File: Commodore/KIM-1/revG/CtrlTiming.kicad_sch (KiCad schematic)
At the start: 22 parts

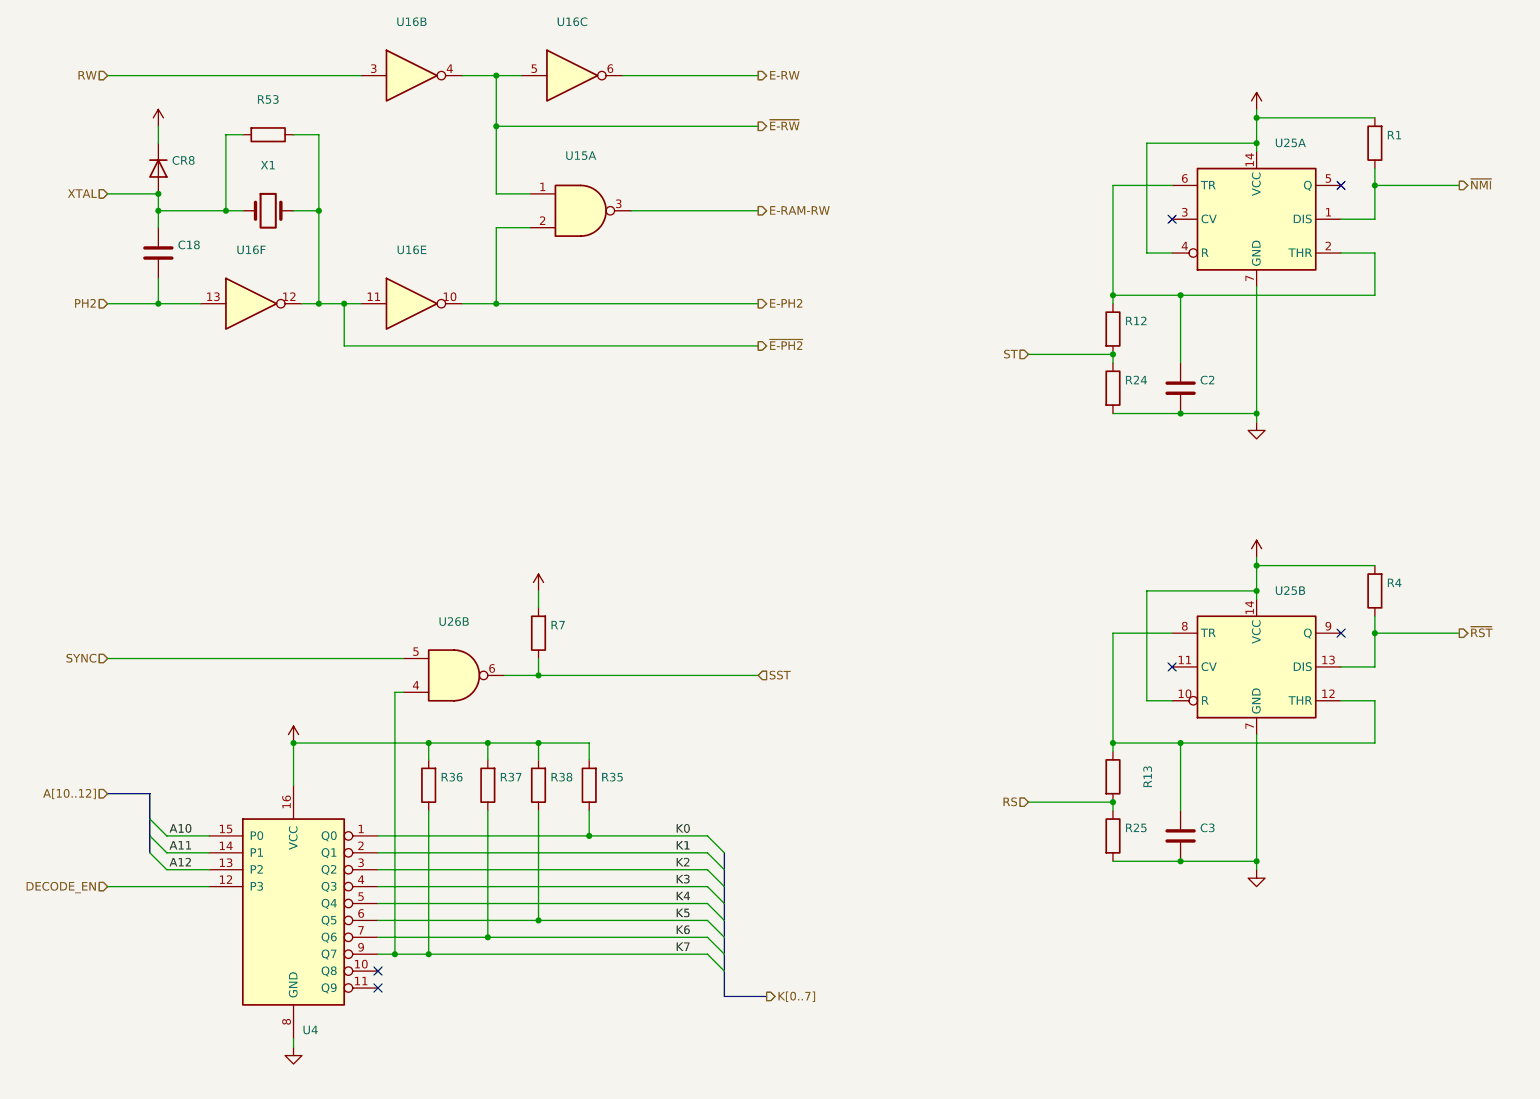
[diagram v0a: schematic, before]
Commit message: Corrected resistor values for R18..R23 and R41..R46 (transposed).
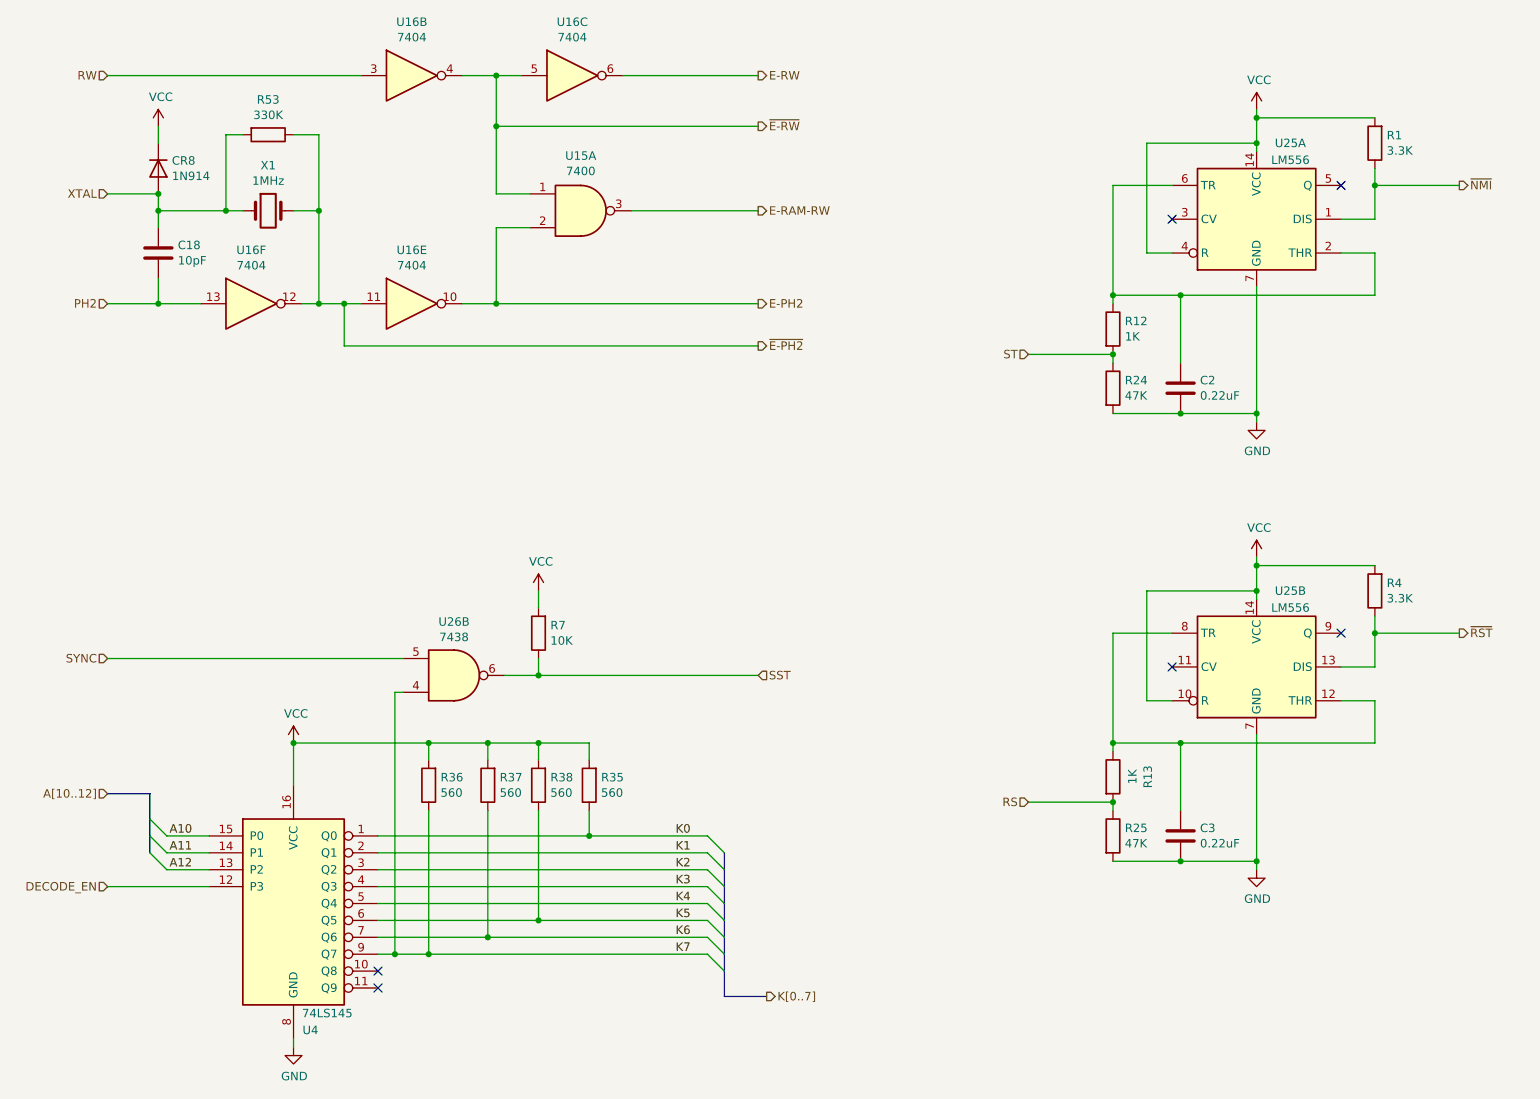
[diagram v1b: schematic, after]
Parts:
- C18: value (none) -> 10pF
- C2, C3: value (none) -> 0.22uF
- CR8: value (none) -> 1N914
- R1, R4: value (none) -> 3.3K
- R12, R13: value (none) -> 1K
- R24, R25: value (none) -> 47K
- R35, R36, R37, R38: value (none) -> 560
- R53: value (none) -> 330K
- R7: value (none) -> 10K
- U15: value (none) -> 7400
- U16: value (none) -> 7404
- U25: value (none) -> LM556
- U26: value (none) -> 7438
- U4: value (none) -> 74LS145
- X1: value (none) -> 1MHz
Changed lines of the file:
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@@
     (in_bom yes) (on_board yes)
     (property "Reference" "U15" (id 0) (at 107.95 41.275 0))
-    (property "Value" "" (id 1) (at 107.95 43.5864 0))
+    (property "Value" "7400" (id 1) (at 107.95 43.5864 0))
     (property "Footprint" "" (id 2) (at 107.95 49.53 0)
       (effects (font (size 1.27 1.27)) hide)
@@
     (in_bom yes) (on_board yes)
     (property "Reference" "U16" (id 0) (at 82.55 21.1582 0))
-    (property "Value" "" (id 1) (at 82.55 23.4696 0))
+    (property "Value" "7404" (id 1) (at 82.55 23.4696 0))
     (property "Footprint" "" (id 2) (at 82.55 29.21 0)
       (effects (font (size 1.27 1.27)) hide)
@@
     (in_bom yes) (on_board yes)
     (property "Reference" "U16" (id 0) (at 106.68 21.1582 0))
-    (property "Value" "" (id 1) (at 106.68 23.4696 0))
+    (property "Value" "7404" (id 1) (at 106.68 23.4696 0))
     (property "Footprint" "" (id 2) (at 106.68 29.21 0)
       (effects (font (size 1.27 1.27)) hide)
@@
     (in_bom yes) (on_board yes)
     (property "Reference" "U16" (id 0) (at 82.55 55.4482 0))
-    (property "Value" "" (id 1) (at 82.55 57.7596 0))
+    (property "Value" "7404" (id 1) (at 82.55 57.7596 0))
     (property "Footprint" "" (id 2) (at 82.55 63.5 0)
       (effects (font (size 1.27 1.27)) hide)
@@
     (in_bom yes) (on_board yes)
     (property "Reference" "U16" (id 0) (at 58.42 55.4482 0))
-    (property "Value" "" (id 1) (at 58.42 57.7596 0))
+    (property "Value" "7404" (id 1) (at 58.42 57.7596 0))
     (property "Footprint" "" (id 2) (at 58.42 63.5 0)
       (effects (font (size 1.27 1.27)) hide)
@@
       (effects (font (size 1.27 1.27)) (justify left))
     )
-    (property "Value" "" (id 1) (at 47.371 57.023 0)
+    (property "Value" "10pF" (id 1) (at 47.371 57.023 0)
       (effects (font (size 1.27 1.27)) (justify left))
     )
@@
       (effects (font (size 1.27 1.27)) (justify left))
     )
-    (property "Value" "" (id 1) (at 46.482 44.323 90)
+    (property "Value" "1N914" (id 1) (at 46.482 44.323 90)
       (effects (font (size 1.27 1.27)) (justify left))
     )
@@
     (in_bom yes) (on_board yes)
     (property "Reference" "X1" (id 0) (at 60.96 42.7228 0))
-    (property "Value" "" (id 1) (at 60.96 45.0342 0))
+    (property "Value" "1MHz" (id 1) (at 60.96 45.0342 0))
     (property "Footprint" "" (id 2) (at 60.96 49.53 0)
       (effects (font (size 1.27 1.27)) hide)
@@
     (in_bom yes) (on_board yes)
     (property "Reference" "R53" (id 0) (at 60.96 32.8422 90))
-    (property "Value" "" (id 1) (at 60.96 35.1536 90))
+    (property "Value" "330K" (id 1) (at 60.96 35.1536 90))
     (property "Footprint" "" (id 2) (at 60.96 36.322 90)
       (effects (font (size 1.27 1.27)) hide)
@@
       (effects (font (size 1.27 1.27)) hide)
     )
-    (property "Value" "" (id 1) (at 44.831 32.4358 0))
+    (property "Value" "VCC" (id 1) (at 44.831 32.4358 0))
     (property "Footprint" "" (id 2) (at 44.45 36.83 0)
       (effects (font (size 1.27 1.27)) hide)
@@
     (in_bom yes) (on_board yes)
     (property "Reference" "U4" (id 0) (at 67.31 172.72 0))
-    (property "Value" "" (id 1) (at 69.85 170.18 0))
+    (property "Value" "74LS145" (id 1) (at 69.85 170.18 0))
     (property "Footprint" "" (id 2) (at 64.77 153.67 0)
       (effects (font (size 1.27 1.27)) hide)
@@
       (effects (font (size 1.27 1.27)) hide)
     )
-    (property "Value" "" (id 1) (at 65.151 125.1458 0))
+    (property "Value" "VCC" (id 1) (at 65.151 125.1458 0))
     (property "Footprint" "" (id 2) (at 64.77 129.54 0)
       (effects (font (size 1.27 1.27)) hide)
@@
       (effects (font (size 1.27 1.27)) hide)
     )
-    (property "Value" "" (id 1) (at 64.897 179.6542 0))
+    (property "Value" "GND" (id 1) (at 64.897 179.6542 0))
     (property "Footprint" "" (id 2) (at 64.77 175.26 0)
       (effects (font (size 1.27 1.27)) hide)
@@
       (effects (font (size 1.27 1.27)) (justify right))
     )
-    (property "Value" "" (id 1) (at 86.868 137.033 0)
+    (property "Value" "560" (id 1) (at 86.868 137.033 0)
       (effects (font (size 1.27 1.27)) (justify right))
     )
@@
       (effects (font (size 1.27 1.27)) (justify right))
     )
-    (property "Value" "" (id 1) (at 95.758 137.033 0)
+    (property "Value" "560" (id 1) (at 95.758 137.033 0)
       (effects (font (size 1.27 1.27)) (justify right))
     )
@@
       (effects (font (size 1.27 1.27)) (justify right))
     )
-    (property "Value" "" (id 1) (at 103.378 137.033 0)
+    (property "Value" "560" (id 1) (at 103.378 137.033 0)
       (effects (font (size 1.27 1.27)) (justify right))
     )
@@
       (effects (font (size 1.27 1.27)) (justify right))
     )
-    (property "Value" "" (id 1) (at 110.998 137.033 0)
+    (property "Value" "560" (id 1) (at 110.998 137.033 0)
       (effects (font (size 1.27 1.27)) (justify right))
     )
@@
     (in_bom yes) (on_board yes)
     (property "Reference" "U26" (id 0) (at 88.9 111.3282 0))
-    (property "Value" "" (id 1) (at 88.9 113.6396 0))
+    (property "Value" "7438" (id 1) (at 88.9 113.6396 0))
     (property "Footprint" "" (id 2) (at 88.9 119.38 0)
       (effects (font (size 1.27 1.27)) hide)
@@
       (effects (font (size 1.27 1.27)) (justify right))
     )
-    (property "Value" "" (id 1) (at 103.378 114.173 0)
+    (property "Value" "10K" (id 1) (at 103.378 114.173 0)
       (effects (font (size 1.27 1.27)) (justify right))
     )
@@
       (effects (font (size 1.27 1.27)) hide)
     )
-    (property "Value" "" (id 1) (at 101.981 102.2858 0))
+    (property "Value" "VCC" (id 1) (at 101.981 102.2858 0))
     (property "Footprint" "" (id 2) (at 101.6 106.68 0)
       (effects (font (size 1.27 1.27)) hide)
@@
       (effects (font (size 1.27 1.27)) hide)
     )
-    (property "Value" "" (id 1) (at 209.931 97.2058 0))
+    (property "Value" "VCC" (id 1) (at 209.931 97.2058 0))
     (property "Footprint" "" (id 2) (at 209.55 101.6 0)
       (effects (font (size 1.27 1.27)) hide)
@@
     (in_bom yes) (on_board yes)
     (property "Reference" "U25" (id 0) (at 214.63 106.68 0))
-    (property "Value" "" (id 1) (at 214.63 109.22 0))
+    (property "Value" "LM556" (id 1) (at 214.63 109.22 0))
     (property "Footprint" "" (id 2) (at 209.55 118.11 0)
       (effects (font (size 1.27 1.27)) hide)
@@
       (effects (font (size 1.27 1.27)) hide)
     )
-    (property "Value" "" (id 1) (at 209.677 152.9842 0))
+    (property "Value" "GND" (id 1) (at 209.677 152.9842 0))
     (property "Footprint" "" (id 2) (at 209.55 148.59 0)
       (effects (font (size 1.27 1.27)) hide)
@@
       (effects (font (size 1.27 1.27)) (justify right))
     )
-    (property "Value" "" (id 1) (at 229.108 107.823 0)
+    (property "Value" "3.3K" (id 1) (at 229.108 107.823 0)
       (effects (font (size 1.27 1.27)) (justify right))
     )
@@
       (effects (font (size 1.27 1.27)) (justify left))
     )
-    (property "Value" "" (id 1) (at 201.041 144.653 0)
+    (property "Value" "0.22uF" (id 1) (at 201.041 144.653 0)
       (effects (font (size 1.27 1.27)) (justify left))
     )
@@
     (in_bom yes) (on_board yes)
     (property "Reference" "R13" (id 0) (at 193.2178 134.62 90))
-    (property "Value" "" (id 1) (at 190.9064 134.62 90))
+    (property "Value" "1K" (id 1) (at 190.9064 134.62 90))
     (property "Footprint" "" (id 2) (at 186.182 134.62 90)
       (effects (font (size 1.27 1.27)) hide)
@@
       (effects (font (size 1.27 1.27)) (justify left))
     )
-    (property "Value" "" (id 1) (at 189.738 144.653 0)
+    (property "Value" "47K" (id 1) (at 189.738 144.653 0)
       (effects (font (size 1.27 1.27)) (justify left))
     )
@@
       (effects (font (size 1.27 1.27)) hide)
     )
-    (property "Value" "" (id 1) (at 209.931 29.8958 0))
+    (property "Value" "VCC" (id 1) (at 209.931 29.8958 0))
     (property "Footprint" "" (id 2) (at 209.55 34.29 0)
       (effects (font (size 1.27 1.27)) hide)
@@
     (in_bom yes) (on_board yes)
     (property "Reference" "U25" (id 0) (at 214.63 39.37 0))
-    (property "Value" "" (id 1) (at 214.63 41.91 0))
+    (property "Value" "LM556" (id 1) (at 214.63 41.91 0))
     (property "Footprint" "" (id 2) (at 209.55 50.8 0)
       (effects (font (size 1.27 1.27)) hide)
@@
       (effects (font (size 1.27 1.27)) hide)
     )
-    (property "Value" "" (id 1) (at 209.677 85.6742 0))
+    (property "Value" "GND" (id 1) (at 209.677 85.6742 0))
     (property "Footprint" "" (id 2) (at 209.55 81.28 0)
       (effects (font (size 1.27 1.27)) hide)
@@
       (effects (font (size 1.27 1.27)) (justify right))
     )
-    (property "Value" "" (id 1) (at 229.108 40.513 0)
+    (property "Value" "3.3K" (id 1) (at 229.108 40.513 0)
       (effects (font (size 1.27 1.27)) (justify right))
     )
@@
       (effects (font (size 1.27 1.27)) (justify left))
     )
-    (property "Value" "" (id 1) (at 201.041 77.343 0)
+    (property "Value" "0.22uF" (id 1) (at 201.041 77.343 0)
       (effects (font (size 1.27 1.27)) (justify left))
     )
@@
       (effects (font (size 1.27 1.27)) (justify left))
     )
-    (property "Value" "" (id 1) (at 189.738 68.453 0)
+    (property "Value" "1K" (id 1) (at 189.738 68.453 0)
       (effects (font (size 1.27 1.27)) (justify left))
     )
@@
       (effects (font (size 1.27 1.27)) (justify left))
     )
-    (property "Value" "" (id 1) (at 189.738 77.343 0)
-      (effects (font (size 1.27 1.27)) (justify left))
-    )
+    (property "Value" "47K" (id 1) (at 189.738 77.343 0)
+      (effects (font (size 1.27 1.27)) (justify left))
+    )
